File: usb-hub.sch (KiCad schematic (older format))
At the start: 27 parts, among them J1 USB_C_Receptacle_16pin, J5 USB_A socket SMT, U1 fe1-4port-hub, U2 LY2508, Y1 12mhz +-50ppm 16-20pf

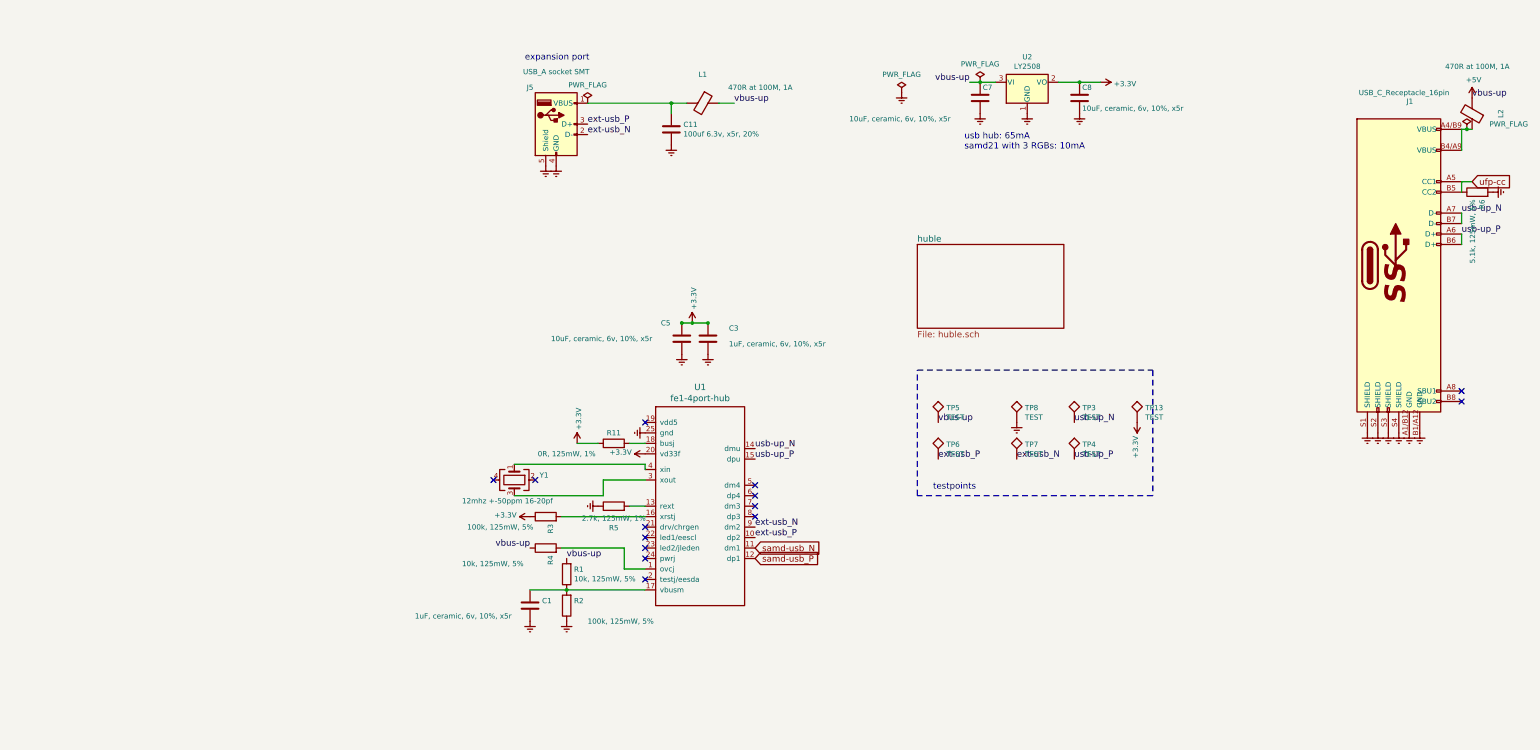
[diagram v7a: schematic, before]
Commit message: removed hub and new board layout
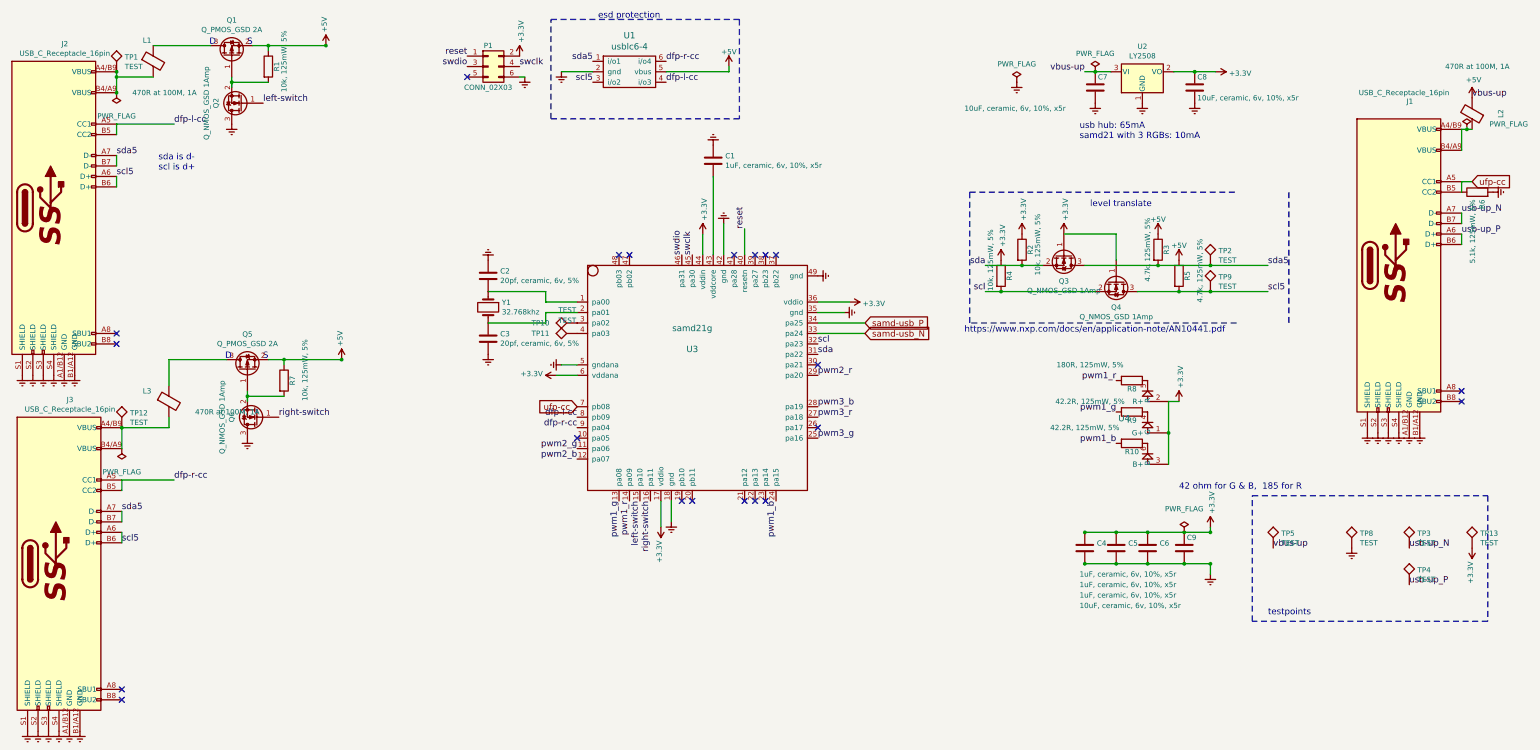
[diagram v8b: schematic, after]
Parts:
- removed C11: 100uf 6.3v, x5r, 20%, raise_fp:C_1206, symbol C
- removed J5: USB_A socket SMT, raise_fp:usb-a-smt-bfriend, symbol USB_A
- removed R11: 0R, 125mW, 1%, raise_fp:R_0603, symbol R
- removed TP6, TP7: TEST, raise_fp:testpoint, symbol TEST
- removed U1: fe1-4port-hub, raise_fp:QFN-24-1EP_4x4mm_Pitch0.5mm, symbol fe1-4port-hub
- removed Y1: 12mhz +-50ppm 16-20pf, raise_fp:Crystal_SMD_3225-4pin_3.2x2.5mm, symbol Crystal_GND24
- added C2: 20pf, ceramic, 6v, 5%, raise_fp:C_0603, symbol C
- added C4, C6: 1uF, ceramic, 6v, 10%, x5r, raise_fp:C_0603, symbol C
- added C9: 10uF, ceramic, 6v, 10%, x5r, raise_fp:C_0603, symbol C
- added J2, J3: USB_C_Receptacle_16pin, raise_fp:usb-c-16smt, symbol USB_C_Receptacle_16pin
- added L3: 470R at 100M, 1A, raise_fp:R_0603, symbol Ferrite_Bead
- added P1: CONN_02X03, raise_fp:Tag-Connect_TC2030-IDC-NL, symbol Conn_02x03_Odd_Even
- added Q1, Q5: Q_PMOS_GSD 2A, raise_fp:SOT-23, symbol Q_PMOS_GSD
- added Q2, Q3, Q4, Q6: Q_NMOS_GSD 1Amp, raise_fp:SOT-323_SC-70, symbol Q_NMOS_GSD
- added R10, R9: 42.2R, 125mW, 5%, raise_fp:R_0603, symbol R
- added R7: 10k, 125mW, 5%, raise_fp:R_0603, symbol R
- added R8: 180R, 125mW, 5%, raise_fp:R_0603, symbol R
- added TP1, TP10, TP11, TP12, TP2, TP9: TEST, raise_fp:testpoint, symbol TEST
- added U1: usblc6-4, raise_fp:SOT-23-6, symbol usblc6-4
- added U3: samd21g, raise_fp:QFN-48-1EP_7x7mm_Pitch0.5mm, symbol samd21g
- added U4: 4 pin RGB led, com anode, red: 500mcd 620nm. Gree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, raise_fp:3528-4p, symbol rgbled
- added Y1: 32.768khz, raise_fp:Crystal_SMD_3215-2pin_3.2x1.5mm, symbol Crystal
- C3: value 1uF, ceramic, 6v, 10%, x5r -> 20pf, ceramic, 6v, 5%; farnell # 1865556 -> 1865475
- C5: value 10uF, ceramic, 6v, 10%, x5r -> 1uF, ceramic, 6v, 10%, x5r; MOQ Value -> (none); farnell # 1288201 -> 1865556; leadtime Value -> (none); supplier PN Value -> (none)
- R2: value 100k, 125mW, 5% -> 10k, 125mW, 5%; MOQ Value -> (none); farnell # 2073350 -> 2447230; leadtime Value -> (none); supplier PN Value -> (none)
- R3: value 100k, 125mW, 5% -> 4.7k, 125mW, 5%; farnell # 2073350 -> 1469807
- R5: value 2.7k, 125mW, 1% -> 4.7k, 125mW, 5%; farnell # 2447324 -> 1469807
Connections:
- net +3V3: now also R2.1, R4.1, C4.1, C6.1, C9.1, P1.2 (Pin_2), Q3.1 (G), Q4.1 (G), U3.17 (vddio), U3.36 (vddio), U3.44 (vddin), U3.6 (vddana), U4.1 (G+), U4.2 (R+), U4.3 (B+); no longer C3.1, R3.1
- net +5V: now also R1.1, R3.1, R5.1, Q1.2 (S), Q5.2 (S), R7.1, U1.5 (vbus); no longer L1.1, R1.2, R4.1
- net Earth: now also C1.1, C2.1, C4.2, C6.2, C9.2, J2.A1/B12 (GND), J2.B1/A12 (GND), J2.S1 (SHIELD), J2.S2 (SHIELD), J2.S3 (SHIELD), J2.S4 (SHIELD), J3.A1/B12 (GND), J3.B1/A12 (GND), J3.S1 (SHIELD), J3.S2 (SHIELD), J3.S3 (SHIELD), J3.S4 (SHIELD), P1.6 (Pin_6), Q2.3 (D), Q6.3 (D), U1.2 (gnd), U3.18 (gnd), U3.35 (gnd), U3.42 (gnd), U3.49 (gnd), U3.5 (gndana); no longer C1.2, R2.1, R5.1
- net samd-usb_N: now also U3.33 (pa24)
- net samd-usb_P: now also U3.34 (pa25)
- net ufp-cc: now also U3.7 (pb08)
- net at L1.2: now also J2.A4/B9 (VBUS), J2.B4/A9 (VBUS), TP1.1
- net scl5: now reaches R5.2
- net scl5: now also J2.A6 (D+), J2.B6 (D+), J3.A6 (D+), J3.B6 (D+), Q4.3 (D), TP9.1, U1.3 (i/o2)
- net scl: now reaches R4.2
- net scl: now also Q4.2 (S), U3.32 (pa23)
- net sda5: now reaches R3.2
- net sda5: now also J2.A7 (D-), J2.B7 (D-), J3.A7 (D-), J3.B7 (D-), Q3.3 (D), TP2.1, U1.1 (i/o1)
- new net: R9.1, U4.4 (G-)
- new net: R8.1, U4.5 (R-)
- new net: R10.1, U4.6 (B-)
- new net: C3.1, U3.2 (pa01), Y1.2
- new net: C2.2, U3.1 (pa00), Y1.1
- new net: TP10.1, U3.3 (pa02)
- new net: TP11.1, U3.4 (pa03)
- new net: J3.A4/B9 (VBUS), J3.B4/A9 (VBUS), L3.2, TP12.1
- new net: C1.2, U3.43 (vddcore)
- new net: Q1.1 (G), Q2.2 (S), R1.2
- new net: L1.1, Q1.3 (D)
- new net: Q5.1 (G), Q6.2 (S), R7.2
- new net: L3.1, Q5.3 (D)
- new net dfp-l-cc: J2.A5 (CC1), J2.B5 (CC2), U1.4 (i/o3), U3.8 (pb09)
- new net dfp-r-cc: J3.A5 (CC1), J3.B5 (CC2), U1.6 (i/o4), U3.9 (pa04)
- new net left-switch: Q2.1 (G), U3.15 (pa10)
- new net pwm1_b: R10.2, U3.24 (pa15)
- new net pwm1_g: R9.2, U3.13 (pa08)
- new net pwm1_r: R8.2, U3.14 (pa09)
- new net pwm2_b: U3.12 (pa07)
- new net pwm2_g: U3.11 (pa06)
- new net pwm2_r: U3.29 (pa20)
- new net pwm3_b: U3.28 (pa19)
- new net pwm3_g: U3.25 (pa16)
- new net pwm3_r: U3.27 (pa18)
- new net reset: P1.1 (Pin_1), U3.40 (resetn)
- new net right-switch: Q6.1 (G), U3.16 (pa11)
- new net sda: Q3.2 (S), R2.2, U3.31 (pa22)
- new net swclk: P1.4 (Pin_4), U3.45 (pa30)
- new net swdio: P1.3 (Pin_3), U3.46 (pa31)
- no-connect marks 14 -> 21
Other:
- note added: "42 ohm for G & B, 185 for R"
- note added: "D"
- note added: "S"
- note added: "esd protection"
- note added: "https://www.nxp.com/docs/en/application-note/AN10441.pdf"
- note added: "level translate\n"
- note added: "sda is d-\nscl is d+"
- note removed: "expansion port"
- moved on the sheet: C7, C8, TP13, TP3, TP4, TP5, TP8, U2
